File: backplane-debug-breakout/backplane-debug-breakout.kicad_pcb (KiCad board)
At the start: 2 copper layers, 65 x 60.5 mm, 21 parts, among them J1 Conn_02x08_Odd_Even, J2 Conn_01x04, J4 Conn_01x02_Socket, J5 Conn_01x04, J6 629105150521, SW1 SW_Push_DPDT, SW2 SW_Omron_B3FS, SW3 EG1218, U1 UMFT234XF

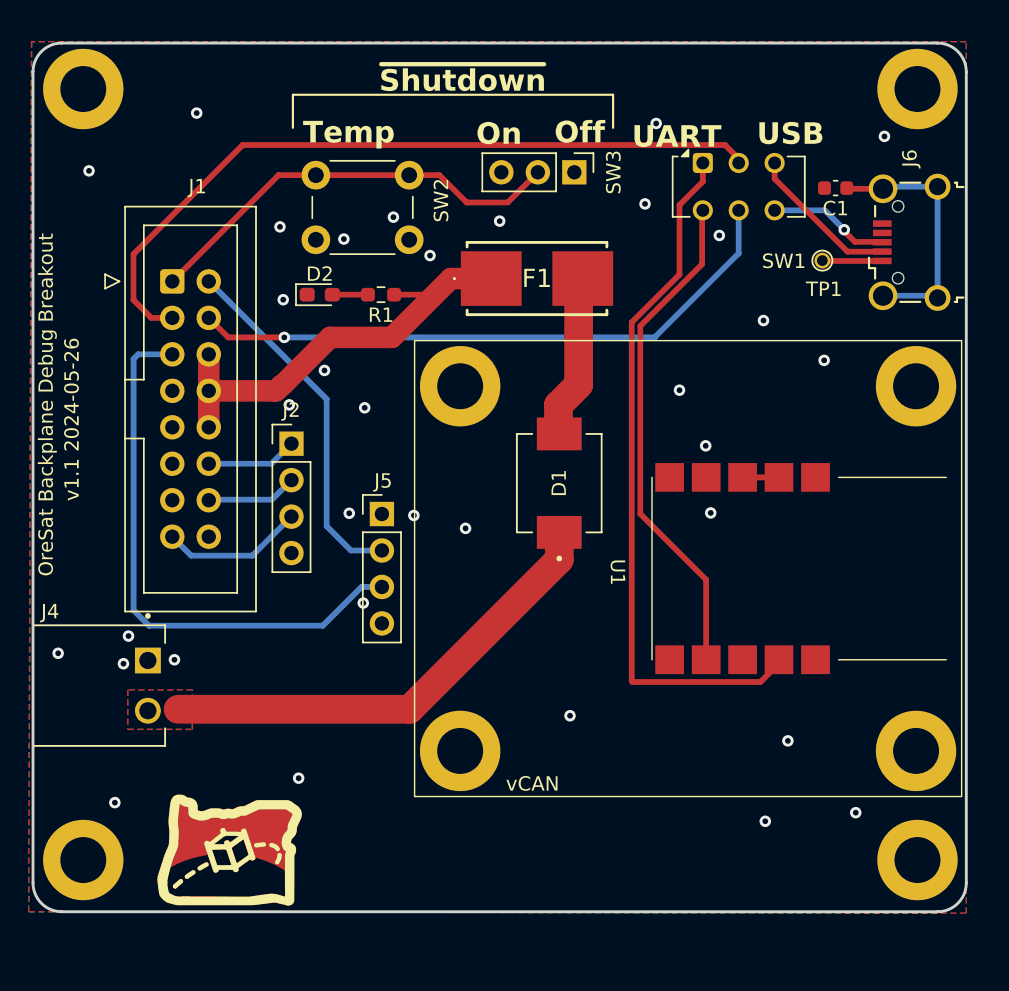
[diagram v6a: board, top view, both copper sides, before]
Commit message: Board polish; updated design rules, made all inputs on the right, centered oresat connector, etc etc. Still needs an actual DPDT switch.
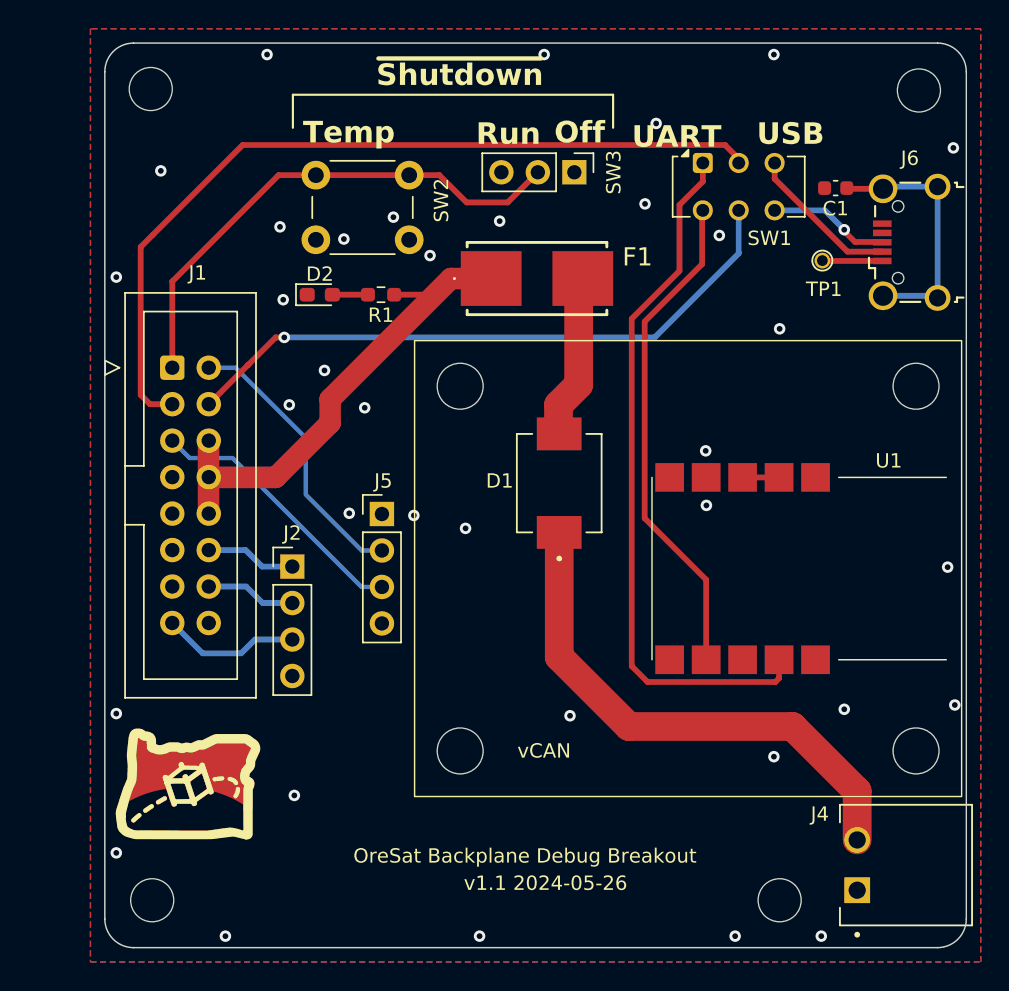
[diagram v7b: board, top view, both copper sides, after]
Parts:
- removed ? (x4): , 
- added H1: MountingHole, oresat-misc:MountingHole_3mm_no_copper, F.Cu at (105.2, 57.2)
- added H2: MountingHole, oresat-misc:MountingHole_3mm_no_copper, F.Cu at (158.7, 57.3)
- added H3: MountingHole, oresat-misc:MountingHole_3mm_no_copper, F.Cu at (105.3, 113.7)
- added H4: MountingHole, oresat-misc:MountingHole_3mm_no_copper, F.Cu at (149.0, 113.7)
- moved J4 68.7 mm to (162.4, 115.5), turned to 90 degrees
- moved J2 8.56 mm to (115.1, 90.5)
- moved J1 6.01 mm to (106.7, 76.6)
- moved Logo 5.44 mm to (107.7, 105.3)
- renumbered REF** to Logo
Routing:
- net /CAN_H: track 39.2 -> 18.8 mm
- net /SD: track 30.2 -> 36.2 mm
- net /C3-UART-TX: track 52.4 -> 58.1 mm
- net /CAN_L: track 25.0 -> 19.6 mm
- net Net-(D1-A): track 32.8 -> 36.7 mm
- net /VBUS: track 30.6 -> 34.1 mm
- net /C3-UART-RX: track 42.9 -> 44.3 mm
- net GND: vias 34 -> 36
- removed copper zone on B.Cu, net Net-(D1-A)
- removed copper zone on F.Cu, net Net-(D1-A)
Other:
- board size 65 x 60.5 mm -> 60 x 63 mm
- board text added: "Run"
- board text removed: "On"

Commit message: chose DPDT for backplane debug breakout and finished BOM
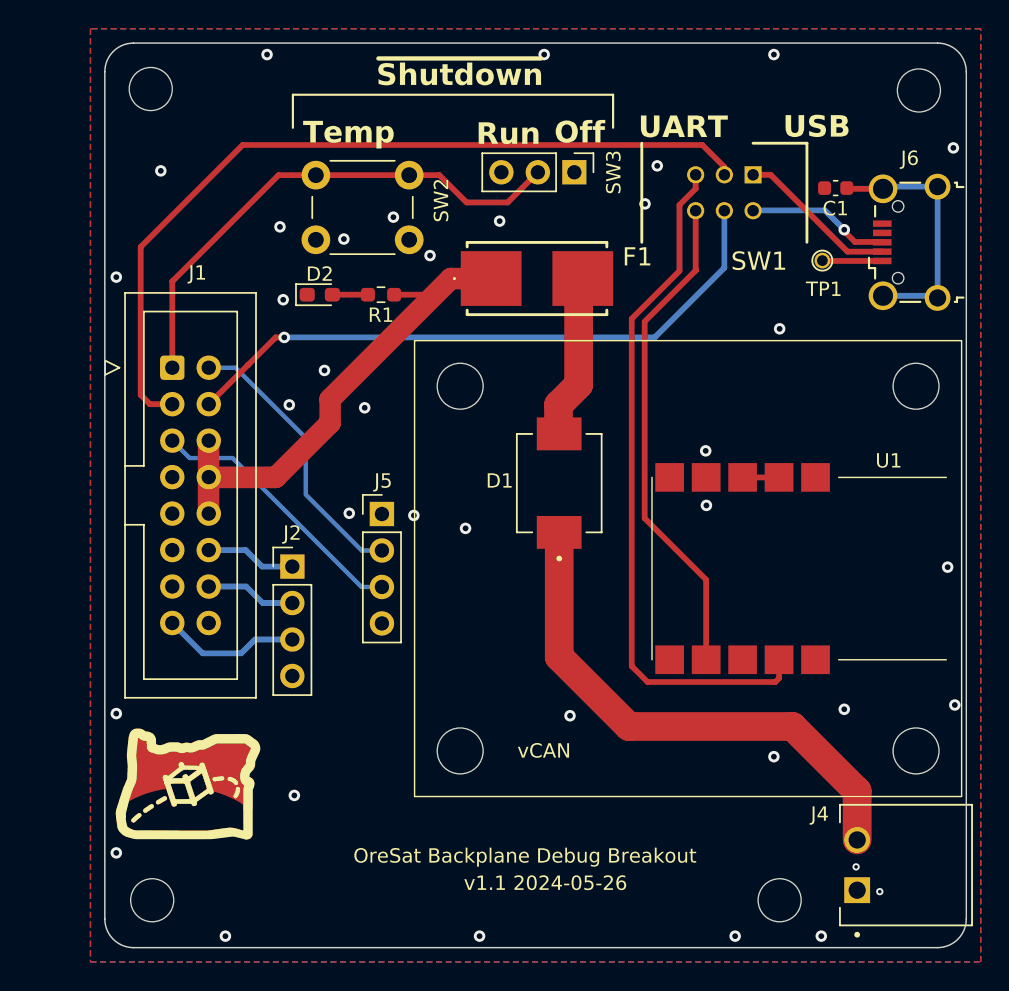
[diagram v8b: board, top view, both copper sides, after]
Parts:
- SW1: footprint oresat-passives:DPDT slide switch 6 pin -> oresat-passives:EG2209 DPDT
- moved SW1 6.40 mm to (147.2, 63.2), turned to -90 degrees
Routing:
- net Net-(J6-D+): track 8.52 -> 10.0 mm
- net Net-(U1-RXD): track 49.2 -> 48.2 mm
- net Net-(J6-D-): track 10.7 -> 11.2 mm
- net /C3-UART-TX: track 58.1 -> 57.5 mm
- net GND: vias 36 -> 37
